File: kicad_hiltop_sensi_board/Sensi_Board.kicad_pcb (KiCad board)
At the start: 4 copper layers, 159.9 x 99.9 mm, 418 parts, among them J1 Conn_02x06_Counter_Clockwise, J10 Conn_ARM_JTAG_SWD_10, J2 Conn_02x06_Counter_Clockwise, J3 Conn_03x32_DIN41612, J4 Conn_02x06_Counter_Clockwise, J5 Conn_02x06_Counter_Clockwise, J6 Conn_02x06_Counter_Clockwise, J7 Conn_02x06_Counter_Clockwise, J8 Conn_02x06_Counter_Clockwise, K1 HRS1KH-S, Q10 ZXMN6A07F, Q11 ZXMN6A07F, Q2 ZXMN6A07F, Q7 ZXMN6A07F, Q8 ZXMN6A07F, SW1 SW_Push, SW2 SW_DIP_x04, SW3 SW_DIP_x04, SW4 SW_DIP_x04, SW5 SW_DIP_x04, U1 INA250A4, U10 MAX31865, U11 MAX31865, U13 CP2102N-A01-GQFN24, U14 BTS4140N, U15 BTS4140N, U16 MAX4194, U17 BTS4140N, U18 BTS4140N, U19 MAX4194, U2 LD1117S33TR_SOT223, U20 MAX4194, U21 MAX4194, U22 STM32F072RBTx, U23 MAX4194, U24 MAX4194, U25 MAX4194, U26 MAX4194, U27 USB2502, U3 AT25DN512CSSHF-B, U4 AD8646, U5 AD8646, U6 LM75B, U7 AT24C02C-SSHM-T, U8 MAX31865, U9 MAX31865, Y1 50ppm 24.000MHZ, Y2 8MHZ, Y3 ABS25-32.768KHZ-6-T

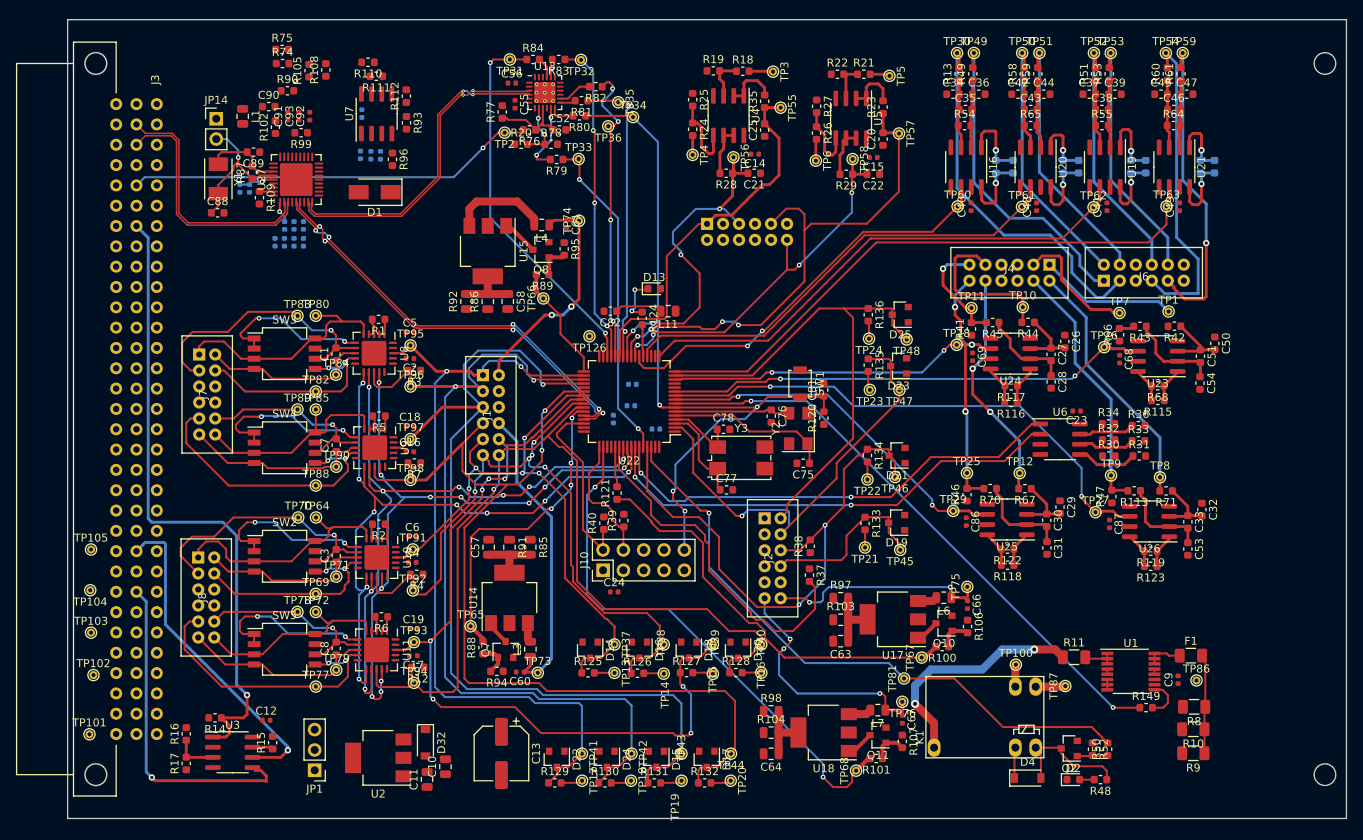
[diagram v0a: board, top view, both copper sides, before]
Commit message: Most major connections complete and differential tracking done on the Sensi board layout
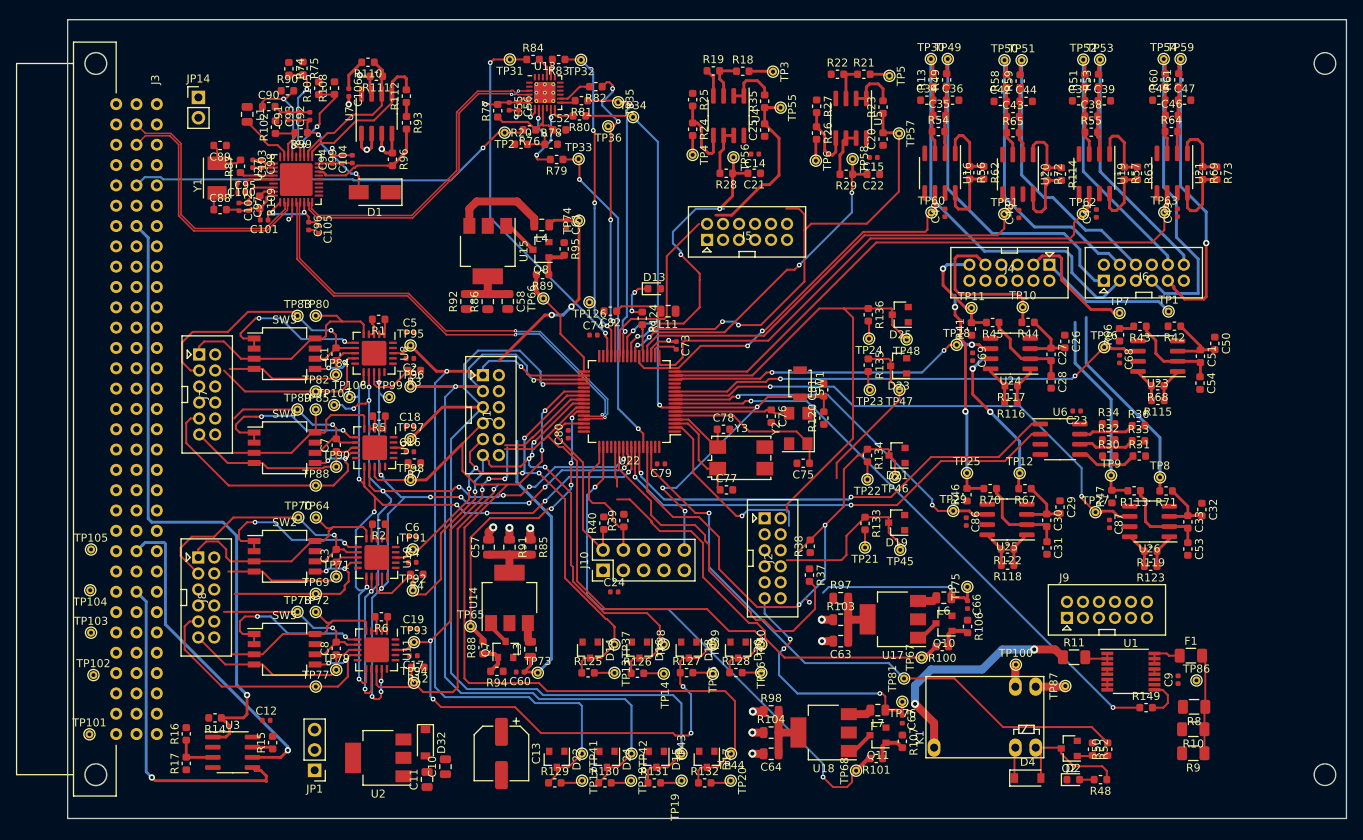
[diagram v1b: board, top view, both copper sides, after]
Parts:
- removed R121: 0R, Resistor_SMD:R_0603_1608Metric
- added J9: Conn_02x06_Counter_Clockwise, Devtank_PCB_Lib:Molex2x06, F.Cu at (185.0, 118.8)
- added TP106: Test_Point, TestPoint:TestPoint_THTPad_D1.0mm_Drill0.5mm, F.Cu at (90.3, 92.2)
- added TP107: Test_Point, TestPoint:TestPoint_THTPad_D1.0mm_Drill0.5mm, F.Cu at (88.4, 93.2)
- added TP99: Test_Point, TestPoint:TestPoint_THTPad_D1.0mm_Drill0.5mm, F.Cu at (95.3, 92.2)
- C100, C101, C102, C103, C104, C105, C106, C73, C74, C79, C80, C94, C95, C96, C97, C98, C99, J5, R114, R56, R57, R62, R63, R69, R72, R73: moved to F.Cu
- moved C103 10.6 mm to (78.2, 63.1), turned to 270 degrees
- moved C74 9.99 mm to (120.8, 84.5), turned to 0 degrees
- moved C98 9.95 mm to (79.3, 63.1), turned to 270 degrees
- moved C102 8.18 mm to (76.5, 68.5), turned to 270 degrees
- moved C97 8.18 mm to (77.7, 68.5), turned to 270 degrees
- moved C73 7.31 mm to (131.2, 85.8), turned to 270 degrees
- moved C94 6.05 mm to (88.2, 62.6)
- moved C80 5.95 mm to (117.7, 96.9), turned to 90 degrees
- moved C101 4.96 mm to (79.6, 70.1), turned to 180 degrees
- moved C79 4.40 mm to (129.2, 100.6)
- moved C105 4.26 mm to (86.4, 71.3)
- moved C89 4.25 mm to (74.1, 60.8)
- moved TP126 4.25 mm to (120.3, 80.4)
- moved R62 3.74 mm to (169.6, 64.2)
- moved C99 3.67 mm to (89.3, 62.6)
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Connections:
- net +12V_EXT renamed /OUT1_NO
- J5 pad 1: /ADC7 -> (no net)
- J5 pad 10: (no net) -> /ADC13
- J5 pad 12: /ADC6 -> /ADC7
- J5 pad 2: GND -> (no net)
- J5 pad 3: /ADC13 -> (no net)
- J5 pad 4: GND -> (no net)
- J5 pad 5: /ADC12 -> GND
- J5 pad 6: GND -> /ADC6
- J5 pad 7: (no net) -> GND
- J5 pad 8: (no net) -> /ADC12
- J5 pad 9: (no net) -> GND
- J6 pad 10: /F3+ -> /F2-
- J6 pad 11: /F3- -> /F2+
- J6 pad 7: /F2+ -> /F3-
- J6 pad 8: /F2- -> /F3+
- U22 pad 53: Net-(R121-Pad2) -> /HS_CTRL_SW3
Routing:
- net GND: track 1.30 -> 56.3 mm, vias 0 -> 10
- net +3V3: track 2.71 -> 39.7 mm, vias 1 -> 5
- net Net-(R112-Pad2): track 0.00 -> 19.3 mm
- net Net-(R110-Pad1): track 0.00 -> 18.2 mm
- net Net-(C91-Pad1): track 0.00 -> 15.7 mm, vias 0 -> 2
- net Net-(R93-Pad2): track 0.00 -> 15.3 mm
- net Net-(C90-Pad1): track 0.00 -> 12.9 mm, vias 0 -> 2
- net Net-(R74-Pad2): track 0.00 -> 12.8 mm, vias 0 -> 2
- net Net-(C88-Pad1): track 18.2 -> 6.56 mm, vias 1 -> 0
- net Net-(R105-Pad1): track 0.00 -> 11.4 mm, vias 0 -> 2
- net /GPIO11: track 56.2 -> 44.8 mm
- net /TH4+: track 29.2 -> 19.8 mm
- net /TH2-: track 32.3 -> 24.9 mm
- net Net-(L1-Pad2): track 0.00 -> 6.98 mm
- net /TH2+: track 32.0 -> 25.5 mm
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
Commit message: Most routing on Sensi Board complete
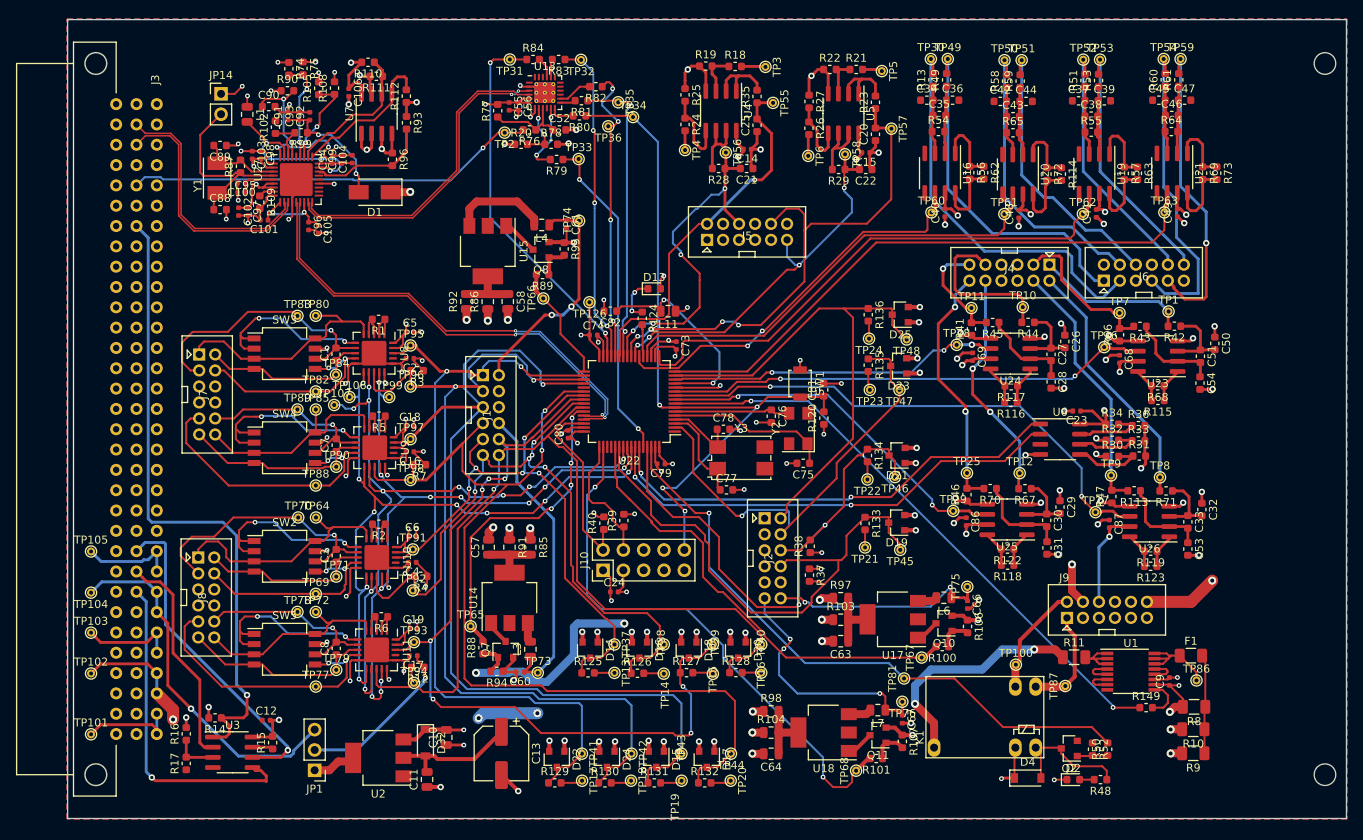
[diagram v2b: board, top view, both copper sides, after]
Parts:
- moved C10 3.65 mm to (102.4, 134.8)
- moved JP14 2.86 mm to (74.2, 54.4)
- moved C21 1.12 mm to (139.9, 63.7)
- moved R28 1.12 mm to (136.4, 63.7)
- moved R29 1.12 mm to (151.4, 63.8)
- moved C14 1.12 mm to (140.0, 61.3)
- moved R22 1.12 mm to (150.3, 51.3)
- moved R26 1.12 mm to (147.7, 58.6)
- moved TP5 1.12 mm to (156.8, 51.5)
- moved TP56 1.12 mm to (137.3, 61.7)
- moved C15 1.12 mm to (154.8, 61.7)
- moved C22 1.12 mm to (154.8, 63.8)
- moved C20 1.12 mm to (156.1, 59.4)
- moved C25 1.12 mm to (141.2, 58.3)
- moved R18 1.12 mm to (138.5, 50.9)
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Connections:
- J1 pad 10: /HS_OUT1 -> GND
- J1 pad 11: /GPIO3 -> GND
- J1 pad 12: /GPIO4 -> /HS_OUT2
- J1 pad 7: /HS_OUT2 -> /GPIO4
- J1 pad 8: GND -> /GPIO3
- J1 pad 9: GND -> /HS_OUT1
- J2 pad 10: /GPIO9 -> /GPIO10
- J2 pad 11: GND -> /GPIO11
- J2 pad 12: /HS_OUT3 -> /GPIO12
- J2 pad 7: /GPIO12 -> /HS_OUT3
- J2 pad 8: /GPIO11 -> GND
- J2 pad 9: /GPIO10 -> /GPIO9
- J4 pad 11: /TH4+ -> /TH2-
- J4 pad 12: /TH4- -> /TH2+
- J4 pad 7: /TH2+ -> /TH4-
- J4 pad 8: /TH2- -> /TH4+
- J7 pad 11: /RTD4_R+ -> /RTD3_F-
- J7 pad 12: /RTD4_F+ -> /RTD3_R-
- J7 pad 7: /RTD3_R- -> /RTD4_F+
- J7 pad 8: /RTD3_F- -> /RTD4_R+
- J8 pad 11: /RTD2_R+ -> /RTD1_F-
- J8 pad 12: /RTD2_F+ -> /RTD1_R-
- J8 pad 7: /RTD1_R- -> /RTD2_F+
- J8 pad 8: /RTD1_F- -> /RTD2_R+
- J9 pad 1: /OUT1_NO -> /OUT1_NC
- J9 pad 10: GND -> +3V3
- J9 pad 12: +5V -> /OUT1_NO
- J9 pad 2: /OUT1_NC -> ADJ_DC
- J9 pad 3: ADJ_DC -> (no net)
- J9 pad 4: +12V -> (no net)
- J9 pad 5: +3V3 -> GND
- J9 pad 6: GND -> (no net)
- J9 pad 7: (no net) -> +5V
- J9 pad 8: (no net) -> GND
- J9 pad 9: (no net) -> +12V
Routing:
- net +5V: track 3.85 -> 357.0 mm, vias 0 -> 9
- net GND: track 56.3 -> 303.5 mm, vias 10 -> 112
- net +12V: track 2.80 -> 243.6 mm, vias 2 -> 7
- net ADJ_DC: track 4.31 -> 231.4 mm, vias 3 -> 5
- net +3V3: track 39.7 -> 222.8 mm, vias 5 -> 59
- net -5V: track 0.51 -> 151.4 mm, vias 0 -> 3
- net +3V3_BP: track 0.00 -> 45.1 mm, vias 0 -> 1
- net /SPI0_MISO: track 0.00 -> 27.5 mm
- net +3V3_LOC: track 0.00 -> 21.5 mm
- net Net-(C82-Pad1): track 6.00 -> 26.2 mm, vias 0 -> 2
- net Net-(C88-Pad1): track 6.56 -> 24.3 mm
- net Net-(L1-Pad2): track 6.98 -> 22.4 mm, vias 0 -> 2
- net Net-(C104-Pad1): track 4.19 -> 15.9 mm, vias 0 -> 2
- net /GPIO11: track 44.8 -> 56.2 mm
- net /OUT1_NO: track 2.77 -> 13.9 mm
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- added copper zone on In2.Cu, net +3V3
- added copper zone on B.Cu, net GND
- added copper zone on F.Cu, net GND
- added copper zone on In1.Cu, net GND
- added copper zone on In2.Cu, net GND

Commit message: Pre stitching via for sensi board.
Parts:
- U27: footprint Package_DFN_QFN:QFN-36-1EP_6x6mm_P0.5mm_EP4.1x4.1mm -> Package_DFN_QFN:QFN-36-1EP_6x6mm_P0.5mm_EP3.7x3.7mm
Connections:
- Y2 pad 2: (no net) -> GND
- Y2 pad 4: (no net) -> GND
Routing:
- net +3V3_BP: track 45.1 -> 64.8 mm, vias 1 -> 2
- net GND: track 303.5 -> 310.1 mm, vias 112 -> 118

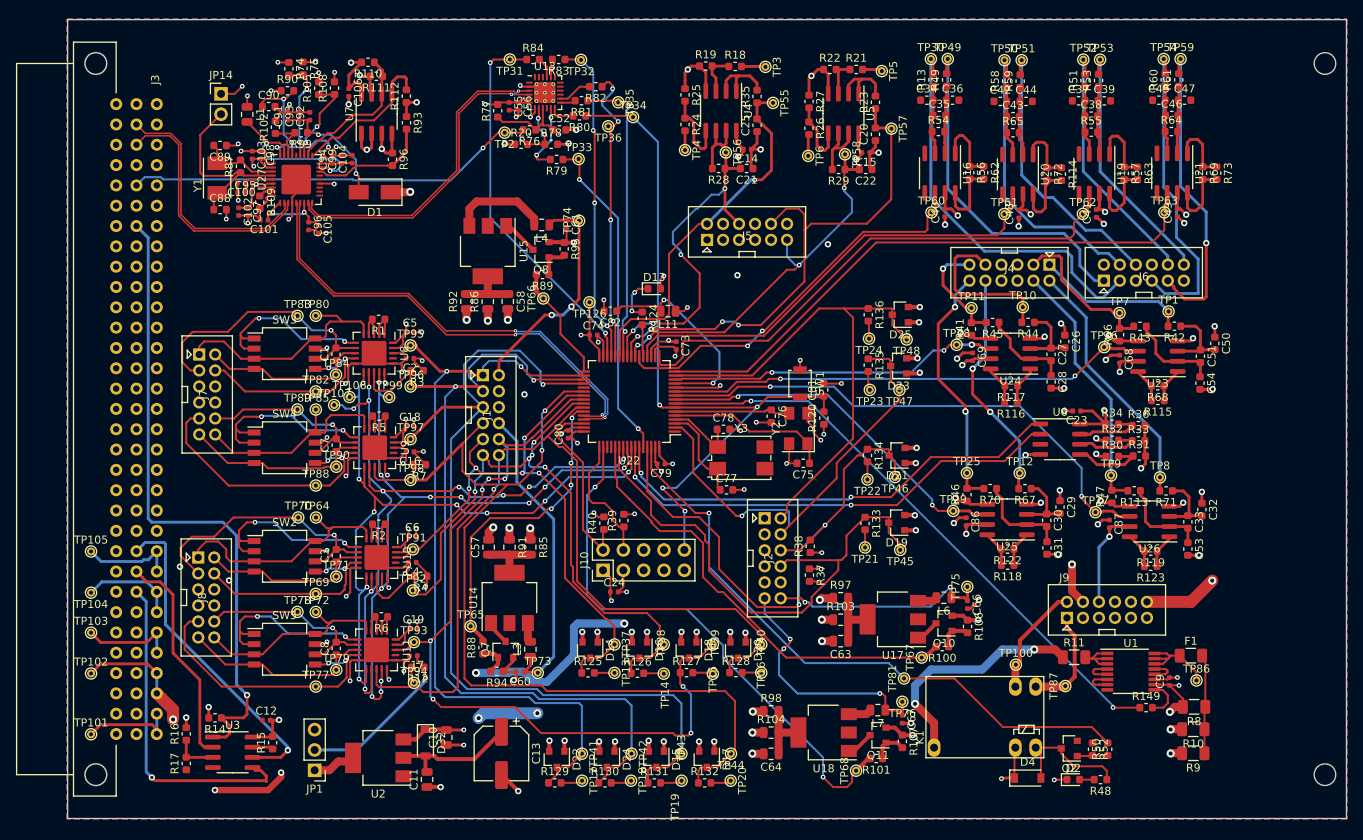
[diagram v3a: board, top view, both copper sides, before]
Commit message: Sensi board with references visible and without stitching vias
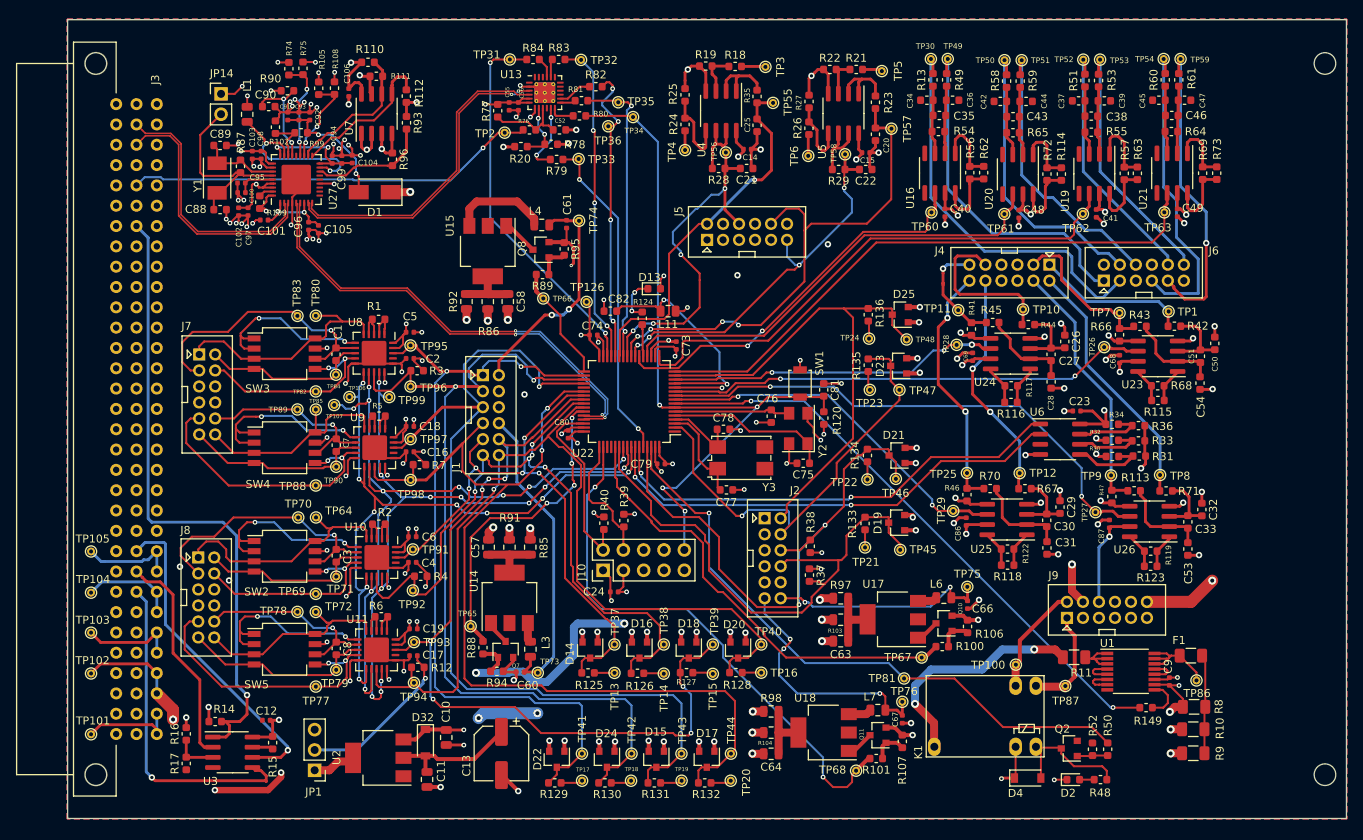
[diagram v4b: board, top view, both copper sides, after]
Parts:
- moved TP11 1.67 mm to (166.4, 81.4)
- moved R14 0.46 mm to (73.5, 132.8)
- moved TP126 0.36 mm to (119.9, 80.3)
- moved R20 0.29 mm to (111.7, 60.9)
- moved TP8 0.29 mm to (191.6, 102.0)
- moved R44 0.28 mm to (175.2, 83.2)
- moved TP10 0.28 mm to (174.5, 81.3)
- moved TP46 0.24 mm to (158.6, 102.5)
- moved K1 0.11 mm to (163.4, 136.0)
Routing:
- net GND: track 310.1 -> 335.6 mm, vias 118 -> 137
- net Net-(C82-Pad1): track 26.2 -> 28.2 mm
- net Net-(C104-Pad1): track 15.9 -> 14.4 mm
- net /STM_USB_DATA_N: track 57.6 -> 56.7 mm
- net /STM_USB_DATA_P: track 58.1 -> 57.2 mm
- net /USB_DATA_N: track 31.6 -> 32.3 mm
- net /USB_DATA_P: track 31.1 -> 31.8 mm
- net /GPIO7: track 116.0 -> 116.7 mm

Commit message: Sensi board complete waiting for review
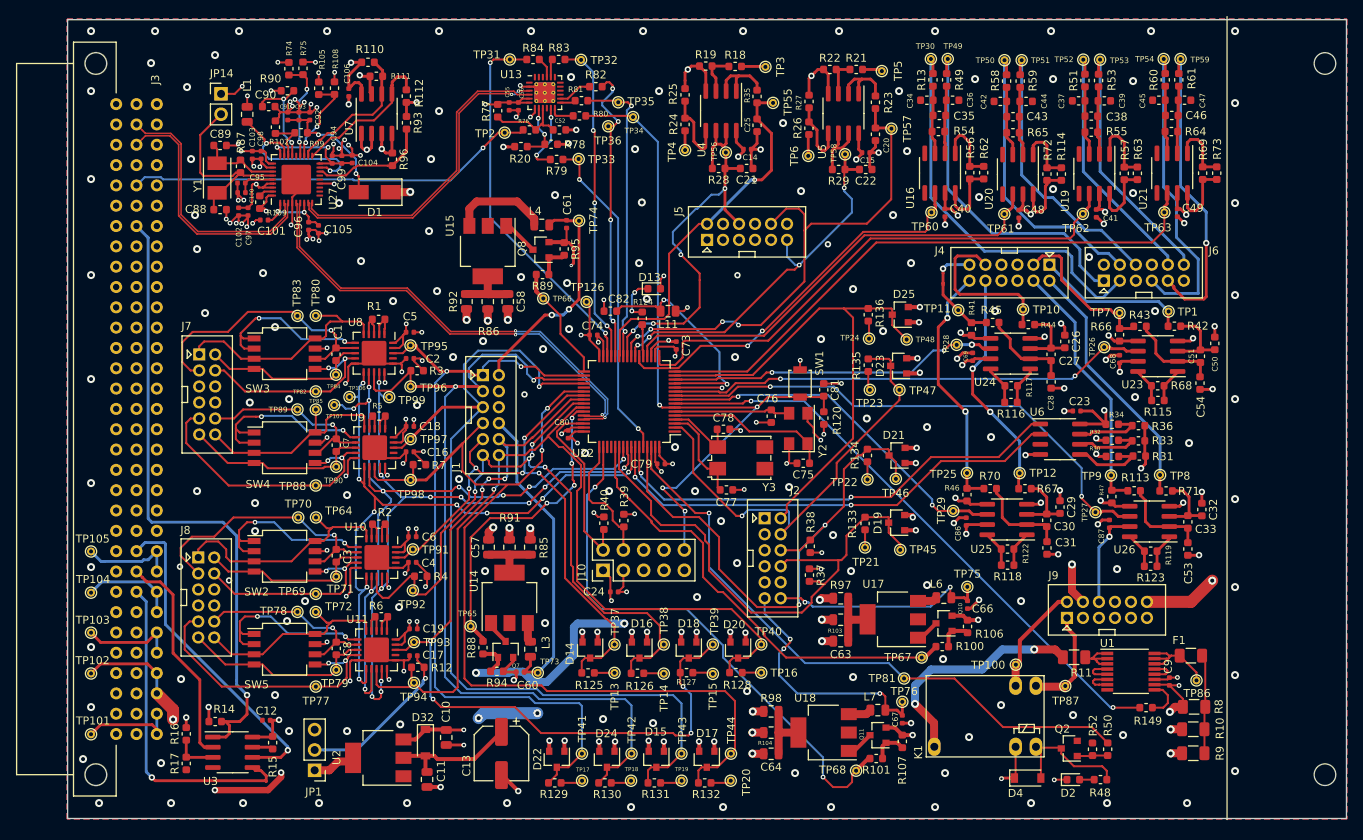
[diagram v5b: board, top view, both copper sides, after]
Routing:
- net GND: vias 137 -> 277
- net (no net): vias 0 -> 1
